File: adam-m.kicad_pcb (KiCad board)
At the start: 2 copper layers, 114.5 x 95.3 mm, 21 parts, among them J1 AudioJack4dpb, SW1 SW_Push, SW10 SW_Push, SW11 SW_Push, SW12 SW_Push, SW13 SW_Push, SW14 SW_Push, SW15 SW_Push, SW16 SW_Push, SW17 SW_Push, SW2 SW_Push, SW3 SW_Push, SW4 SW_Push, SW5 SW_Push, SW6 SW_Push, SW7 SW_Push, SW8 SW_Push, SW9 SW_Push, U1 ProMicro-pinout

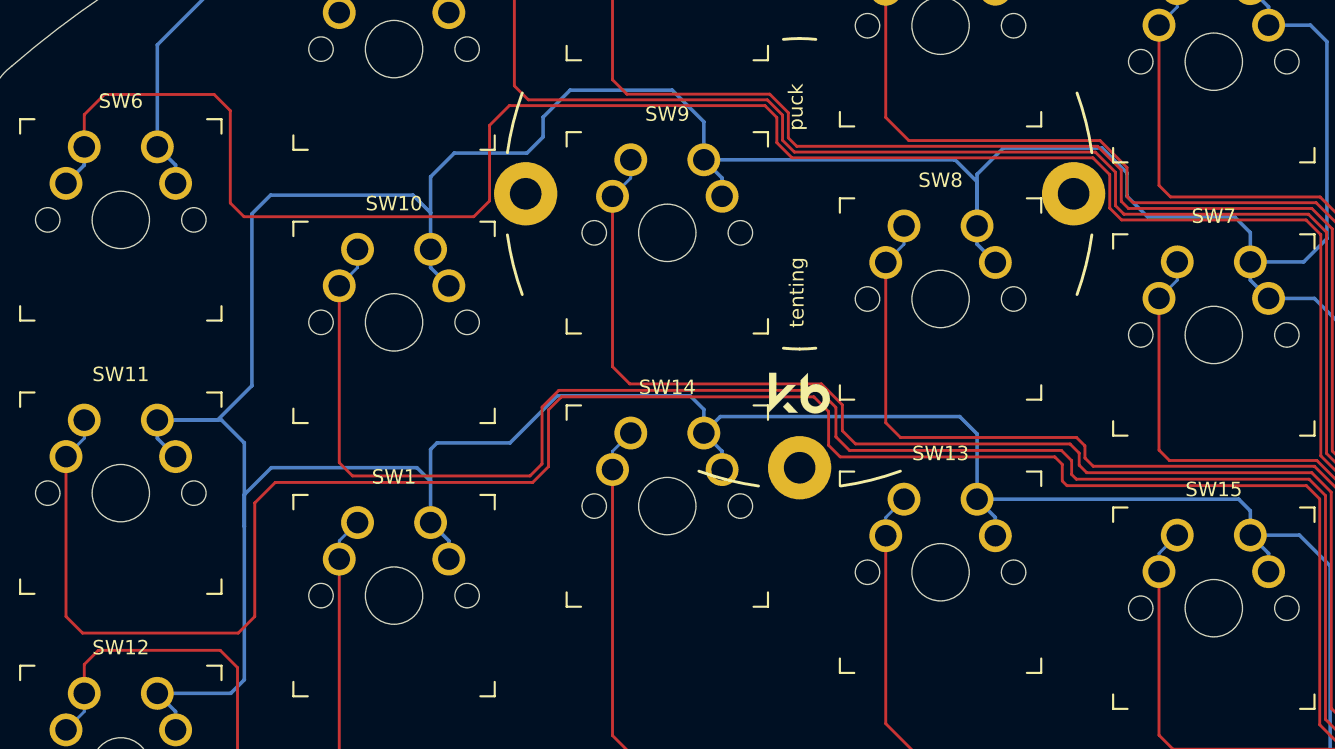
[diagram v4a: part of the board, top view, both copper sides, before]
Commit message: rework switch numbering, rearrange schematic for clarity
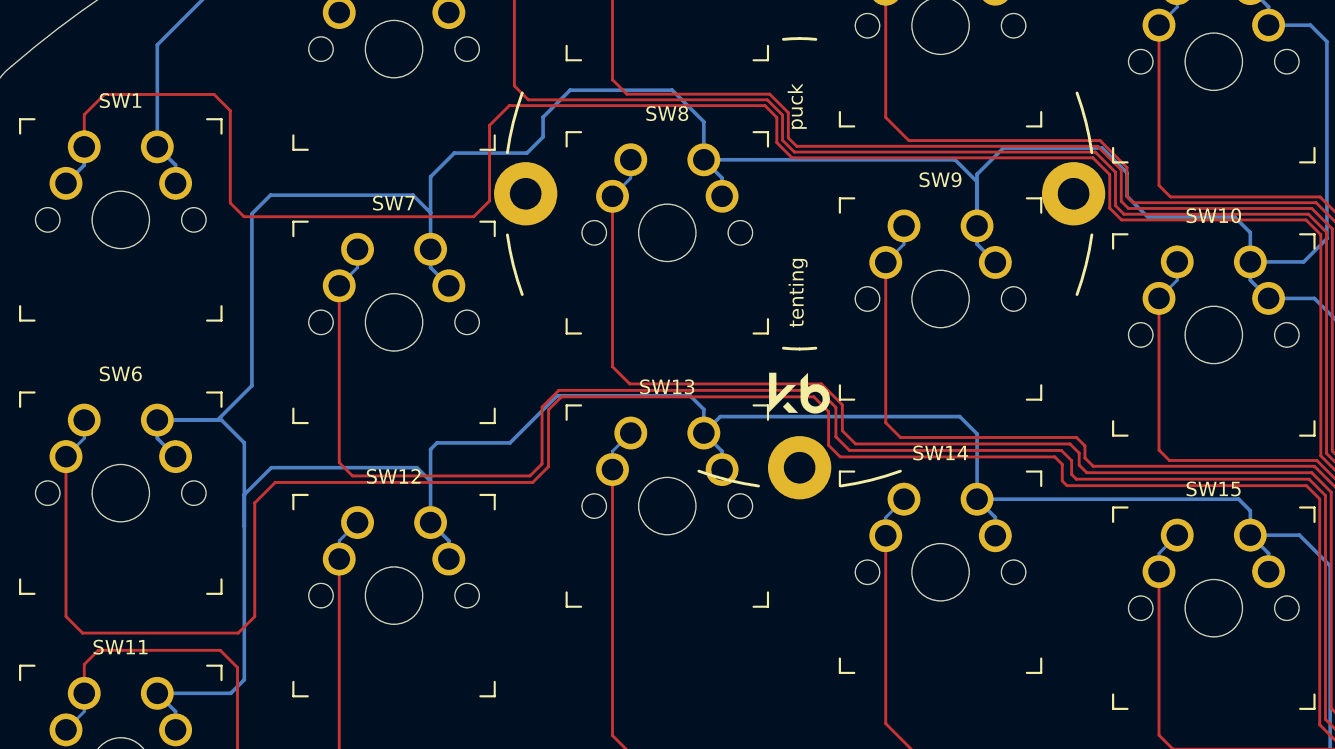
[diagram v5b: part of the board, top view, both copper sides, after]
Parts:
- renumbered SW6 to SW1, SW7 to SW10, SW12 to SW11, SW1 to SW12, SW14 to SW13, SW13 to SW14, SW11 to SW6, SW10 to SW7, SW9 to SW8, SW8 to SW9
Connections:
- SW1 pad 1: Switch6 -> Switch1
- SW10 pad 1: Switch7 -> Switch10
- SW11 pad 1: Switch15 -> Switch11
- SW12 pad 1: Switch1 -> Switch12
- SW13 pad 1: Switch14 -> Switch13
- SW14 pad 1: Switch13 -> Switch14
- SW15 pad 1: Switch12 -> Switch15
- SW6 pad 1: Switch11 -> Switch6
- SW7 pad 1: Switch10 -> Switch7
- SW8 pad 1: Switch9 -> Switch8
- SW9 pad 1: Switch8 -> Switch9
- U1 pad 1: Switch10 -> Switch7
- U1 pad 10: Switch15 -> Switch11
- U1 pad 13: Switch9 -> Switch8
- U1 pad 14: Switch8 -> Switch9
- U1 pad 15: Switch7 -> Switch10
- U1 pad 16: Switch6 -> Switch1
- U1 pad 5: Switch11 -> Switch6
- U1 pad 6: Switch12 -> Switch15
- U1 pad 7: Switch13 -> Switch14
- U1 pad 8: Switch14 -> Switch13
- U1 pad 9: Switch1 -> Switch12
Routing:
- net Switch7: track 43.7 -> 159.1 mm
- net Switch10: track 159.1 -> 43.7 mm
- net Switch15: track 137.6 -> 62.9 mm
- net Switch12: track 62.9 -> 127.3 mm
- net Switch11: track 175.8 -> 137.6 mm
- net Switch6: track 143.2 -> 175.8 mm
- net Switch14: track 110.2 -> 85.1 mm
- net Switch13: track 85.1 -> 110.2 mm
- net Switch9: track 90.5 -> 66.5 mm
- net Switch8: track 66.5 -> 90.5 mm
- net Switch1: track 127.3 -> 143.2 mm

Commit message: Re-assign TRRS pad labels
This is a hacked symbol anyway, may as well make it a logical one. Now
the pad order flows from one end to another of the internal
connections (note that sleeve connection is at opposite end to pin so
*appears* out-of-order on PCB footprint). Also explicitly include pads
that are shorted together by reversible footprint and reflect this in
schematic.
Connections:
- J1 pad B: Switch18 -> vcc
- J1 pad C: gnd -> Data
- J1 pad D: vcc -> gnd
- U1 pad 2: Switch18 -> Data
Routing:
- net Switch18: track 47.8 -> 0.00 mm
- net Data: track 0.00 -> 47.8 mm
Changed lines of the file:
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@@
   (net 18 "Switch17")
   (net 19 "reset")
-  (net 20 "Switch18")
+  (net 20 "Data")
   (net 21 "vcc")
   (net 22 "unconnected-(U1-RAW-Pad24)")
@@
       (net 8 "Switch7") (pinfunction "TX") (pintype "bidirectional"))
     (pad "2" thru_hole circle (at 7.6114 -11.938) (size 1.524 1.524) (drill 0.8128) (layers "*.Cu" "*.Mask")
-      (net 20 "Switch18") (pinfunction "RX") (pintype "bidirectional"))
+      (net 20 "Data") (pinfunction "RX") (pintype "bidirectional"))
     (pad "3" thru_hole circle (at 7.6114 -9.398) (size 1.524 1.524) (drill 0.8128) (layers "*.Cu" "*.Mask")
       (net 1 "gnd") (pinfunction "GND") (pintype "power_in"))
@@
     (pad "" np_thru_hole circle (at 0 1.6 270) (size 0.8 0.8) (drill 0.8) (layers "*.Cu" "*.Mask"))
     (pad "" np_thru_hole circle (at 0 8.6 270) (size 0.8 0.8) (drill 0.8) (layers "*.Cu" "*.Mask"))
-    (pad "B" thru_hole oval (at -2.33 6.22 90) (size 1.6 2) (drill oval 0.9 1.3) (layers "*.Cu" "*.Mask")
-      (net 20 "Switch18") (pintype "passive"))
-    (pad "B" thru_hole oval (at 2.3 6.2 270) (size 1.6 2) (drill oval 0.9 1.3) (layers "*.Cu" "*.Mask")
-      (net 20 "Switch18") (pintype "passive"))
-    (pad "C" thru_hole oval (at -2.33 10.22 90) (size 1.6 2) (drill oval 0.9 1.3) (layers "*.Cu" "*.Mask")
+    (pad "A" thru_hole oval (at -2.3 11.3 270) (size 1.6 2) (drill oval 0.9 1.3) (layers "*.Cu" "*.Mask")
       (net 1 "gnd") (pintype "passive"))
-    (pad "C" thru_hole oval (at -2.3 11.3 270) (size 1.6 2) (drill oval 0.9 1.3) (layers "*.Cu" "*.Mask")
+    (pad "A" thru_hole oval (at 2.27 11.32 90) (size 1.6 2) (drill oval 0.9 1.3) (layers "*.Cu" "*.Mask")
       (net 1 "gnd") (pintype "passive"))
-    (pad "C" thru_hole oval (at 2.27 11.32 90) (size 1.6 2) (drill oval 0.9 1.3) (layers "*.Cu" "*.Mask")
+    (pad "B" thru_hole oval (at -2.33 3.22 90) (size 1.6 2) (drill oval 0.9 1.3) (layers "*.Cu" "*.Mask")
+      (net 21 "vcc") (pintype "passive"))
+    (pad "B" thru_hole oval (at 2.3 3.2 270) (size 1.6 2) (drill oval 0.9 1.3) (layers "*.Cu" "*.Mask")
+      (net 21 "vcc") (pintype "passive"))
+    (pad "C" thru_hole oval (at -2.33 6.22 90) (size 1.6 2) (drill oval 0.9 1.3) (layers "*.Cu" "*.Mask")
+      (net 20 "Data") (pintype "passive"))
+    (pad "C" thru_hole oval (at 2.3 6.2 270) (size 1.6 2) (drill oval 0.9 1.3) (layers "*.Cu" "*.Mask")
+      (net 20 "Data") (pintype "passive"))
+    (pad "D" thru_hole oval (at -2.33 10.22 90) (size 1.6 2) (drill oval 0.9 1.3) (layers "*.Cu" "*.Mask")
       (net 1 "gnd") (pintype "passive"))
-    (pad "C" thru_hole oval (at 2.3 10.2 270) (size 1.6 2) (drill oval 0.9 1.3) (layers "*.Cu" "*.Mask")
+    (pad "D" thru_hole oval (at 2.3 10.2 270) (size 1.6 2) (drill oval 0.9 1.3) (layers "*.Cu" "*.Mask")
       (net 1 "gnd") (pintype "passive"))
-    (pad "D" thru_hole oval (at -2.33 3.22 90) (size 1.6 2) (drill oval 0.9 1.3) (layers "*.Cu" "*.Mask")
-      (net 21 "vcc") (pintype "passive"))
-    (pad "D" thru_hole oval (at 2.3 3.2 270) (size 1.6 2) (drill oval 0.9 1.3) (layers "*.Cu" "*.Mask")
-      (net 21 "vcc") (pintype "passive"))
     (model "/Users/danny/syncproj/kicad-libs/footprints/Keebio-Parts.pretty/3dmodels/PJ-320A.step"
       (offset (xyz 0 0 0))
